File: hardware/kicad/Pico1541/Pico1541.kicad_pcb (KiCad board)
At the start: 2 copper layers, 100 x 76.2 mm, 64 parts, among them J1 SWD, J2 Serial, J3 Display/Keys, J4 Micro SD Card, J5 5V_EXT, J6 USB_A, J7 OLED/Key_Hat, J8 OLED, J9 DIN-6, Q1 MMBT3904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

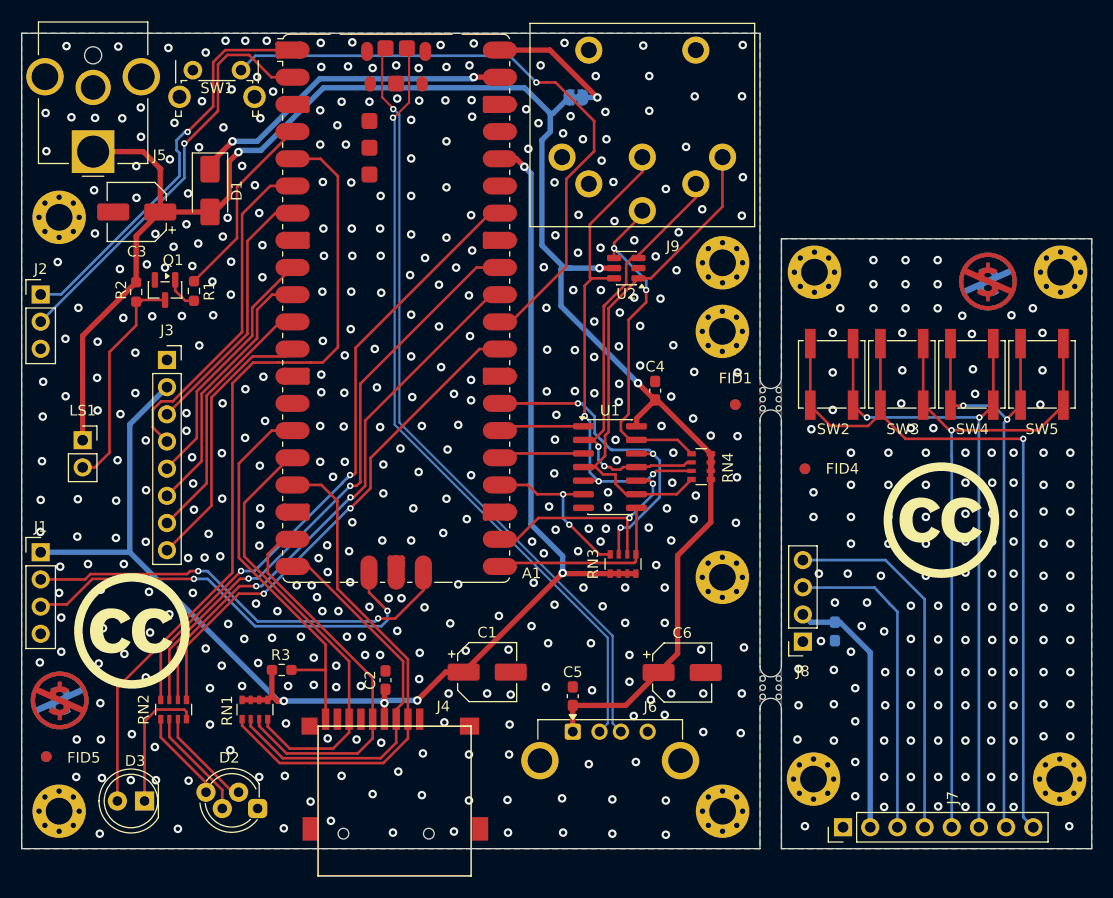
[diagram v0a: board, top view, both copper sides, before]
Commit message: Fixed status test to work Added missing footprint dir for hardware
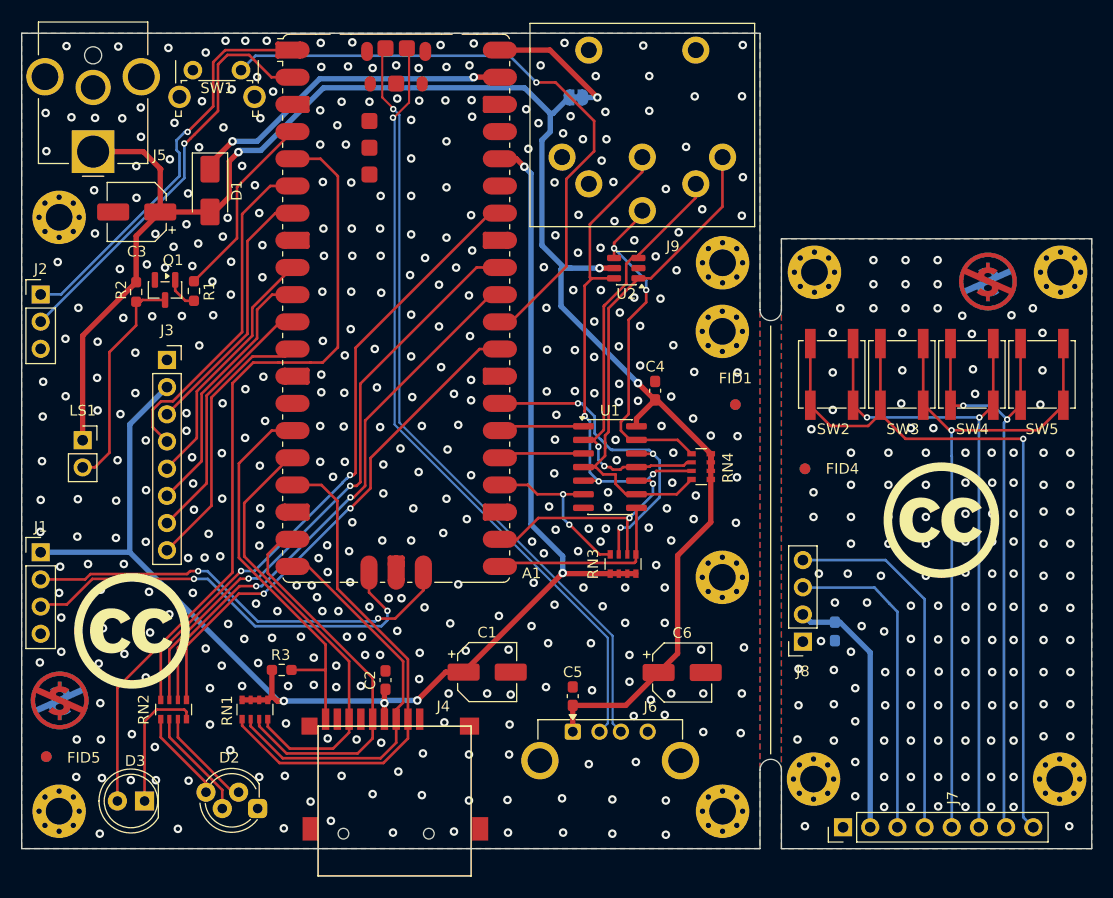
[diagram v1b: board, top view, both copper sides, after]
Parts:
- removed the REF** at (170.0, 87.3)
- removed the REF** at (170.0, 114.3)
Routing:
- net GND: vias 398 -> 399
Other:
- outline, holes or cut-outs redrawn

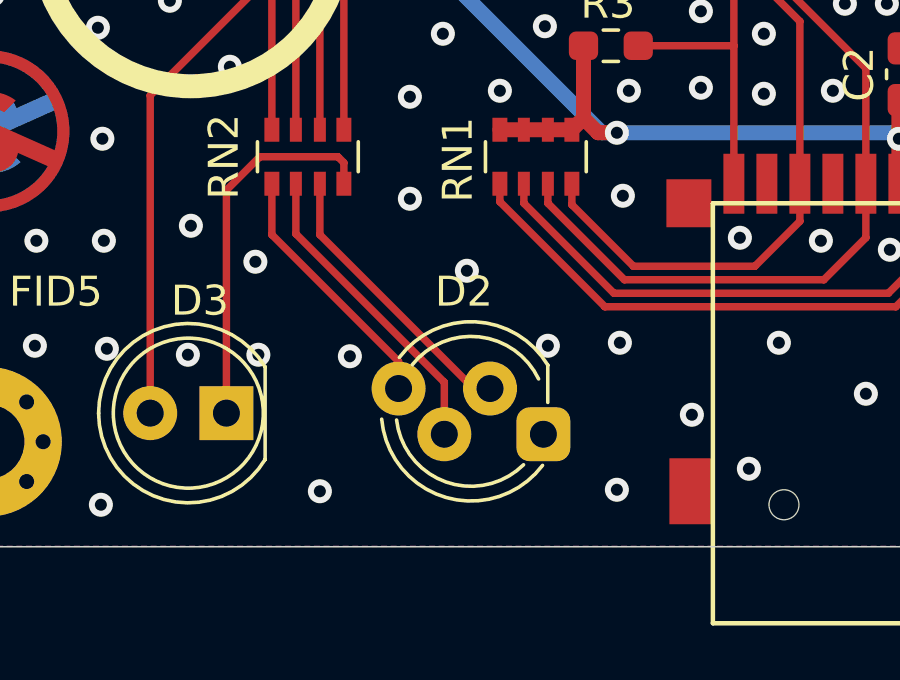
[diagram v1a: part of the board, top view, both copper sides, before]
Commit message: Added support for activity LED.
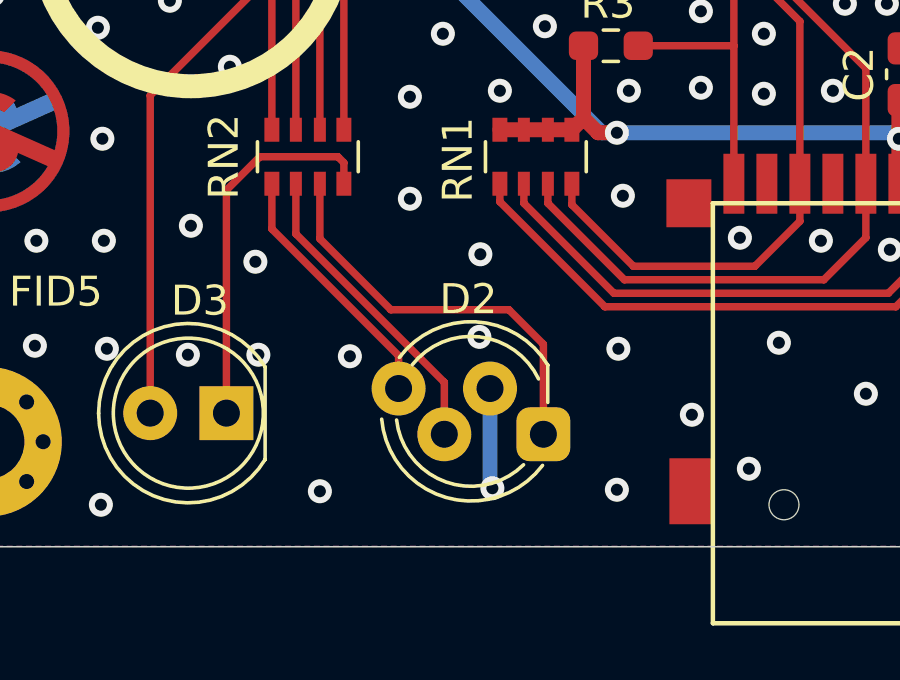
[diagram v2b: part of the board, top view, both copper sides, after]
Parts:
- D2: footprint LED_THT:LED_D5.0mm-4_RGB_Staggered_Pins -> Pico1541-footprints:LED_D5.0mm-4_RGB_CorrectStaggered_Pins
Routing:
- net Net-(D2-RA): track 9.50 -> 13.7 mm
- net GND: track 0.00 -> 3.36 mm, vias 399 -> 400
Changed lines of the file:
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@@
 		)
 	)
-	(footprint "LED_THT:LED_D5.0mm-4_RGB_Staggered_Pins"
+	(footprint "Pico1541-footprints:LED_D5.0mm-4_RGB_CorrectStaggered_Pins"
 		(layer "F.Cu")
 		(at 121.05 125.6 180)
@@
 		(tags "rgb led")
 		(property "Reference" "D2"
-			(at 2.65 4.75 180)
+			(at 2.5 4.5 180)
 			(layer "F.SilkS")
 			(effects
@@
 			)
 		)
-		(pad "1" thru_hole roundrect
-			(at 0 0 180)
+		(pad "1" thru_hole circle
+			(at 1.778 1.524 180)
 			(size 1.8 1.8)
 			(drill 0.9)
 			(layers "*.Cu" "*.Mask")
 			(remove_unused_layers no)
-			(roundrect_rratio 0.25)
 			(net "GND")
 			(pinfunction "K_1")
 			(pintype "passive")
 		)
-		(pad "2" thru_hole circle
-			(at 1.778 1.524 180)
+		(pad "2" thru_hole roundrect
+			(at 0 0 180)
 			(size 1.8 1.8)
 			(drill 0.9)
 			(layers "*.Cu" "*.Mask")
 			(remove_unused_layers no)
+			(roundrect_rratio 0.25)
 			(net "Net-(D2-RA)")
 			(pinfunction "RA_2")
@@
 	)
 	(via
-		(at 121.2 122.65)
-		(size 0.8)
-		(drill 0.4)
-		(layers "F.Cu" "B.Cu")
-		(free yes)
-		(net "GND")
-	)
-	(via
 		(at 112.4 75.05)
 		(size 0.8)
@@
 	)
 	(via
+		(at 119.35 127.4)
+		(size 0.8)
+		(drill 0.4)
+		(layers "F.Cu" "B.Cu")
+		(free yes)
+		(net "GND")
+	)
+	(via
 		(at 121.1 112)
 		(size 0.8)
@@
 	)
 	(via
+		(at 118.915909 122.353607)
+		(size 0.8)
+		(drill 0.4)
+		(layers "F.Cu" "B.Cu")
+		(free yes)
+		(net "GND")
+	)
+	(via
 		(at 136.4 124.35)
 		(size 0.8)
@@
 	)
 	(via
-		(at 123.6 122.55)
+		(at 123.55 122.75)
 		(size 0.8)
 		(drill 0.4)
@@
 	)
 	(via
-		(at 118.5 120.15)
+		(at 118.95 119.6)
 		(size 0.8)
 		(drill 0.4)
@@
 	)
 	(segment
+		(start 119.272 124.076)
+		(end 119.272 127.322)
+		(width 0.5)
+		(layer "B.Cu")
+		(net "GND")
+	)
+	(segment
+		(start 119.272 127.322)
+		(end 119.35 127.4)
+		(width 0.5)
+		(layer "B.Cu")
+		(net "GND")
+	)
+	(segment
 		(start 144.02 102.65)
 		(end 156.25 102.65)
@@
 	)
 	(segment
-		(start 116.224 123.174)
-		(end 112 118.95)
+		(start 116.224 122.979984)
+		(end 112 118.755984)
 		(width 0.25)
 		(layer "F.Cu")
@@
 	(segment
 		(start 116.224 124.076)
-		(end 116.224 123.174)
+		(end 116.224 122.979984)
 		(width 0.25)
 		(layer "F.Cu")
@@
 	)
 	(segment
-		(start 112 118.95)
+		(start 112 118.755984)
 		(end 112 117.25)
 		(width 0.25)
@@
 	)
 	(segment
-		(start 118.726 124.076)
-		(end 119.272 124.076)
+		(start 121.05 122.6)
+		(end 121.05 125.6)
 		(width 0.25)
 		(layer "F.Cu")
@@
 	(segment
 		(start 113.6 117.25)
-		(end 113.6 118.95)
+		(end 113.6 119.083192)
+		(width 0.25)
+		(layer "F.Cu")
+		(net "Net-(D2-RA)")
+	)
+	(segment
+		(start 113.6 119.083192)
+		(end 115.966808 121.45)
+		(width 0.25)
+		(layer "F.Cu")
+		(net "Net-(D2-RA)")
+	)
+	(segment
+		(start 115.966808 121.45)
+		(end 119.9 121.45)
 		(width 0.25)
 		(layer "F.Cu")
@@
 	)
 	(segment
-		(start 113.6 118.95)
-		(end 118.726 124.076)
+		(start 119.9 121.45)
+		(end 121.05 122.6)
 		(width 0.25)
 		(layer "F.Cu")

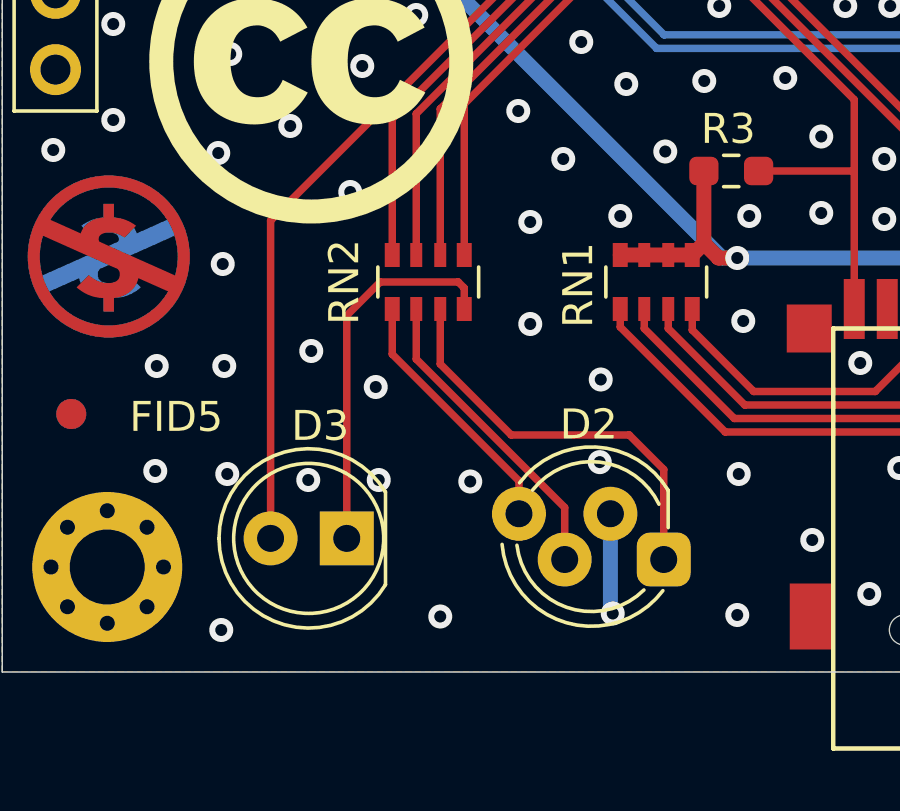
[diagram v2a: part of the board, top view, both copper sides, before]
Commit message: chore(debug): hardcode GPIO 10 to high for logic analyzer wiring test
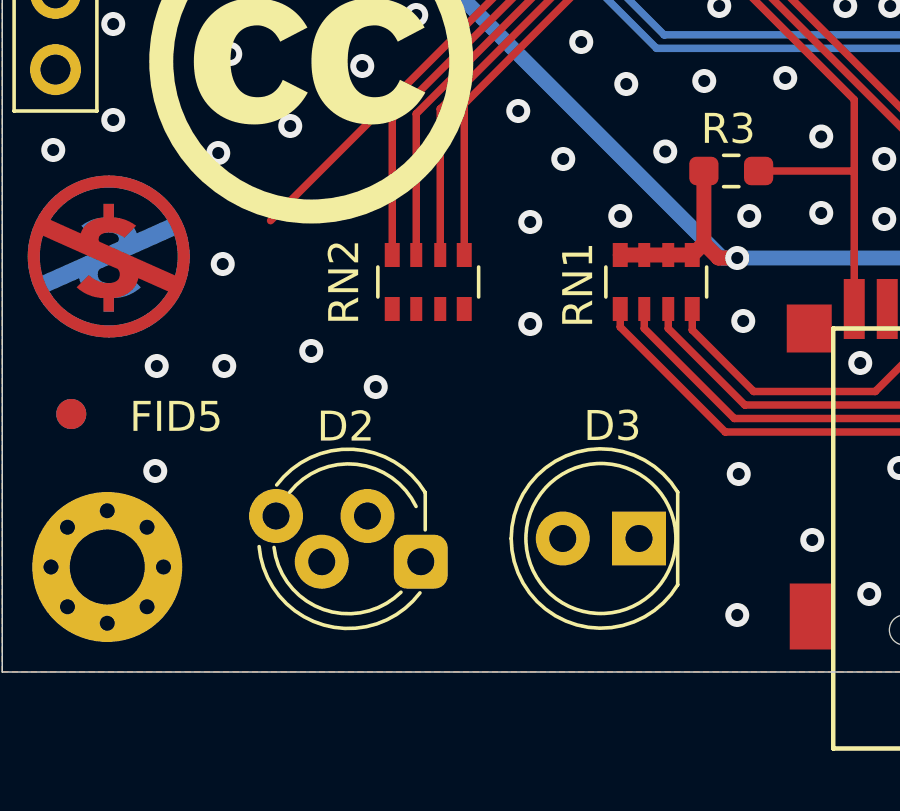
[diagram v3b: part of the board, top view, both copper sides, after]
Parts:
- moved D3 9.74 mm to (120.2, 124.9)
- moved D2 8.10 mm to (113.0, 125.7)
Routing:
- net Net-(D2-RA): track 13.7 -> 0.00 mm
- net Net-(D3-KA): track 12.6 -> 0.00 mm
- net /PLED_N: track 75.6 -> 65.1 mm
- net Net-(D2-GA): track 10.4 -> 0.00 mm
- net Net-(D2-BA): track 8.58 -> 0.00 mm
- net GND: track 3.36 -> 0.00 mm, vias 400 -> 390
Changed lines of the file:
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@@
 	(footprint "LED_THT:LED_D5.0mm"
 		(layer "F.Cu")
-		(at 110.484292 124.896522 180)
+		(at 120.225 124.9 180)
 		(descr "LED, diameter 5.0mm, 2 pins, http://cdn-reichelt.de/documents/datenblatt/A500/LL-504BC2E-009.pdf, generated by kicad-footprint-generator")
 		(tags "LED")
@@
 		)
 		(point
-			(at 109.214292 124.896522)
+			(at 118.955 124.9)
 			(size 2)
 			(layer "F.Fab")
@@
 	(footprint "Pico1541-footprints:LED_D5.0mm-4_RGB_CorrectStaggered_Pins"
 		(layer "F.Cu")
-		(at 121.05 125.6 180)
+		(at 112.952 125.674 180)
 		(descr "LED, diameter 5.0mm, 4 pins, WP154A4, https://www.kingbright.com/attachments/file/psearch/000/00/00/L-154A4SUREQBFZGEW(Ver.11A).pdf")
 		(tags "rgb led")
@@
 	)
 	(via
-		(at 106.3 127.95)
-		(size 0.8)
-		(drill 0.4)
-		(layers "F.Cu" "B.Cu")
-		(free yes)
-		(net "GND")
-	)
-	(via
 		(at 115.5 72.8)
 		(size 0.8)
@@
 	)
 	(via
-		(at 114.6 123)
-		(size 0.8)
-		(drill 0.4)
-		(layers "F.Cu" "B.Cu")
-		(free yes)
-		(net "GND")
-	)
-	(via
 		(at 146.15 60.25)
 		(size 0.8)
@@
 	)
 	(via
-		(at 119.35 127.4)
-		(size 0.8)
-		(drill 0.4)
-		(layers "F.Cu" "B.Cu")
-		(free yes)
-		(net "GND")
-	)
-	(via
 		(at 121.1 112)
 		(size 0.8)
@@
 	)
 	(via
-		(at 111.55 122.95)
-		(size 0.8)
-		(drill 0.4)
-		(layers "F.Cu" "B.Cu")
-		(free yes)
-		(net "GND")
-	)
-	(via
 		(at 126.6 105.85)
 		(size 0.8)
@@
 	)
 	(via
-		(at 118.915909 122.353607)
-		(size 0.8)
-		(drill 0.4)
-		(layers "F.Cu" "B.Cu")
-		(free yes)
-		(net "GND")
-	)
-	(via
 		(at 136.4 124.35)
 		(size 0.8)
@@
 	)
 	(via
-		(at 106.5 122.75)
-		(size 0.8)
-		(drill 0.4)
-		(layers "F.Cu" "B.Cu")
-		(free yes)
-		(net "GND")
-	)
-	(via
 		(at 116.2 54.95)
 		(size 0.8)
@@
 	)
 	(via
-		(at 109.2 122.95)
-		(size 0.8)
-		(drill 0.4)
-		(layers "F.Cu" "B.Cu")
-		(free yes)
-		(net "GND")
-	)
-	(via
 		(at 117.86 61.95)
 		(size 0.8)
@@
 	)
 	(via
-		(at 113.6 127.5)
-		(size 0.8)
-		(drill 0.4)
-		(layers "F.Cu" "B.Cu")
-		(free yes)
-		(net "GND")
-	)
-	(via
 		(at 161.8 98.55)
 		(size 0.8)
@@
 	)
 	(via
-		(at 110.6 113.35)
-		(size 0.8)
-		(drill 0.4)
-		(layers "F.Cu" "B.Cu")
-		(free yes)
-		(net "GND")
-	)
-	(via
 		(at 104.3 78.81)
 		(size 0.8)
@@
 	)
 	(via
-		(at 118.95 119.6)
-		(size 0.8)
-		(drill 0.4)
-		(layers "F.Cu" "B.Cu")
-		(free yes)
-		(net "GND")
-	)
-	(via
 		(at 165.75 98.9)
 		(size 0.8)
@@
 	)
 	(segment
-		(start 119.272 124.076)
-		(end 119.272 127.322)
-		(width 0.5)
-		(layer "B.Cu")
-		(net "GND")
-	)
-	(segment
-		(start 119.272 127.322)
-		(end 119.35 127.4)
-		(width 0.5)
-		(layer "B.Cu")
-		(net "GND")
-	)
-	(segment
 		(start 144.02 102.65)
 		(end 156.25 102.65)
@@
 	)
 	(segment
-		(start 110.484292 117.465708)
-		(end 110.484292 124.896522)
-		(width 0.25)
-		(layer "F.Cu")
-		(net "Net-(D3-KA)")
-	)
-	(segment
-		(start 114.2 116.35)
-		(end 111.6 116.35)
-		(width 0.25)
-		(layer "F.Cu")
-		(net "Net-(D3-KA)")
-	)
-	(segment
-		(start 114.4 117.25)
-		(end 114.4 116.55)
-		(width 0.25)
-		(layer "F.Cu")
-		(net "Net-(D3-KA)")
-	)
-	(segment
-		(start 114.4 116.55)
-		(end 114.2 116.35)
-		(width 0.25)
-		(layer "F.Cu")
-		(net "Net-(D3-KA)")
-	)
-	(segment
-		(start 111.6 116.35)
-		(end 110.484292 117.465708)
-		(width 0.25)
-		(layer "F.Cu")
-		(net "Net-(D3-KA)")
-	)
-	(segment
 		(start 127.125 83.925)
 		(end 128.55 82.5)
@@
 	)
 	(segment
-		(start 107.944292 124.896522)
-		(end 107.944292 114.305708)
-		(width 0.25)
-		(layer "F.Cu")
-		(net "/PLED_N")
-	)
-	(segment
 		(start 128.55 82.5)
 		(end 128.55 66.5)
@@
 	)
 	(segment
-		(start 116.224 122.979984)
-		(end 112 118.755984)
-		(width 0.25)
-		(layer "F.Cu")
-		(net "Net-(D2-BA)")
-	)
-	(segment
-		(start 116.224 124.076)
-		(end 116.224 122.979984)
-		(width 0.25)
-		(layer "F.Cu")
-		(net "Net-(D2-BA)")
-	)
-	(segment
-		(start 112 118.755984)
-		(end 112 117.25)
-		(width 0.25)
-		(layer "F.Cu")
-		(net "Net-(D2-BA)")
-	)
-	(segment
-		(start 117.748 123.867588)
-		(end 112.8 118.919588)
-		(width 0.25)
-		(layer "F.Cu")
-		(net "Net-(D2-GA)")
-	)
-	(segment
-		(start 112.8 118.919588)
-		(end 112.8 117.25)
-		(width 0.25)
-		(layer "F.Cu")
-		(net "Net-(D2-GA)")
-	)
-	(segment
-		(start 117.748 125.6)
-		(end 117.748 123.867588)
-		(width 0.25)
-		(layer "F.Cu")
-		(net "Net-(D2-GA)")
-	)
-	(segment
-		(start 121.05 122.6)
-		(end 121.05 125.6)
-		(width 0.25)
-		(layer "F.Cu")
-		(net "Net-(D2-RA)")
-	)
-	(segment
-		(start 113.6 117.25)
-		(end 113.6 119.083192)
-		(width 0.25)
-		(layer "F.Cu")
-		(net "Net-(D2-RA)")
-	)
-	(segment
-		(start 113.6 119.083192)
-		(end 115.966808 121.45)
-		(width 0.25)
-		(layer "F.Cu")
-		(net "Net-(D2-RA)")
-	)
-	(segment
-		(start 115.966808 121.45)
-		(end 119.9 121.45)
-		(width 0.25)
-		(layer "F.Cu")
-		(net "Net-(D2-RA)")
-	)
-	(segment
-		(start 119.9 121.45)
-		(end 121.05 122.6)
-		(width 0.25)
-		(layer "F.Cu")
-		(net "Net-(D2-RA)")
-	)
-	(segment
